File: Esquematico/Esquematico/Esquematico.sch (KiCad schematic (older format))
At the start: 27 parts, among them P1 Digital, P10 CONN_01X01, P11 CONN_01X01, P12 CONN_01X01, P13 CONN_01X01, P2 Power, P3 Analog, P4 Analog, P5 PWM, P6 PWM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

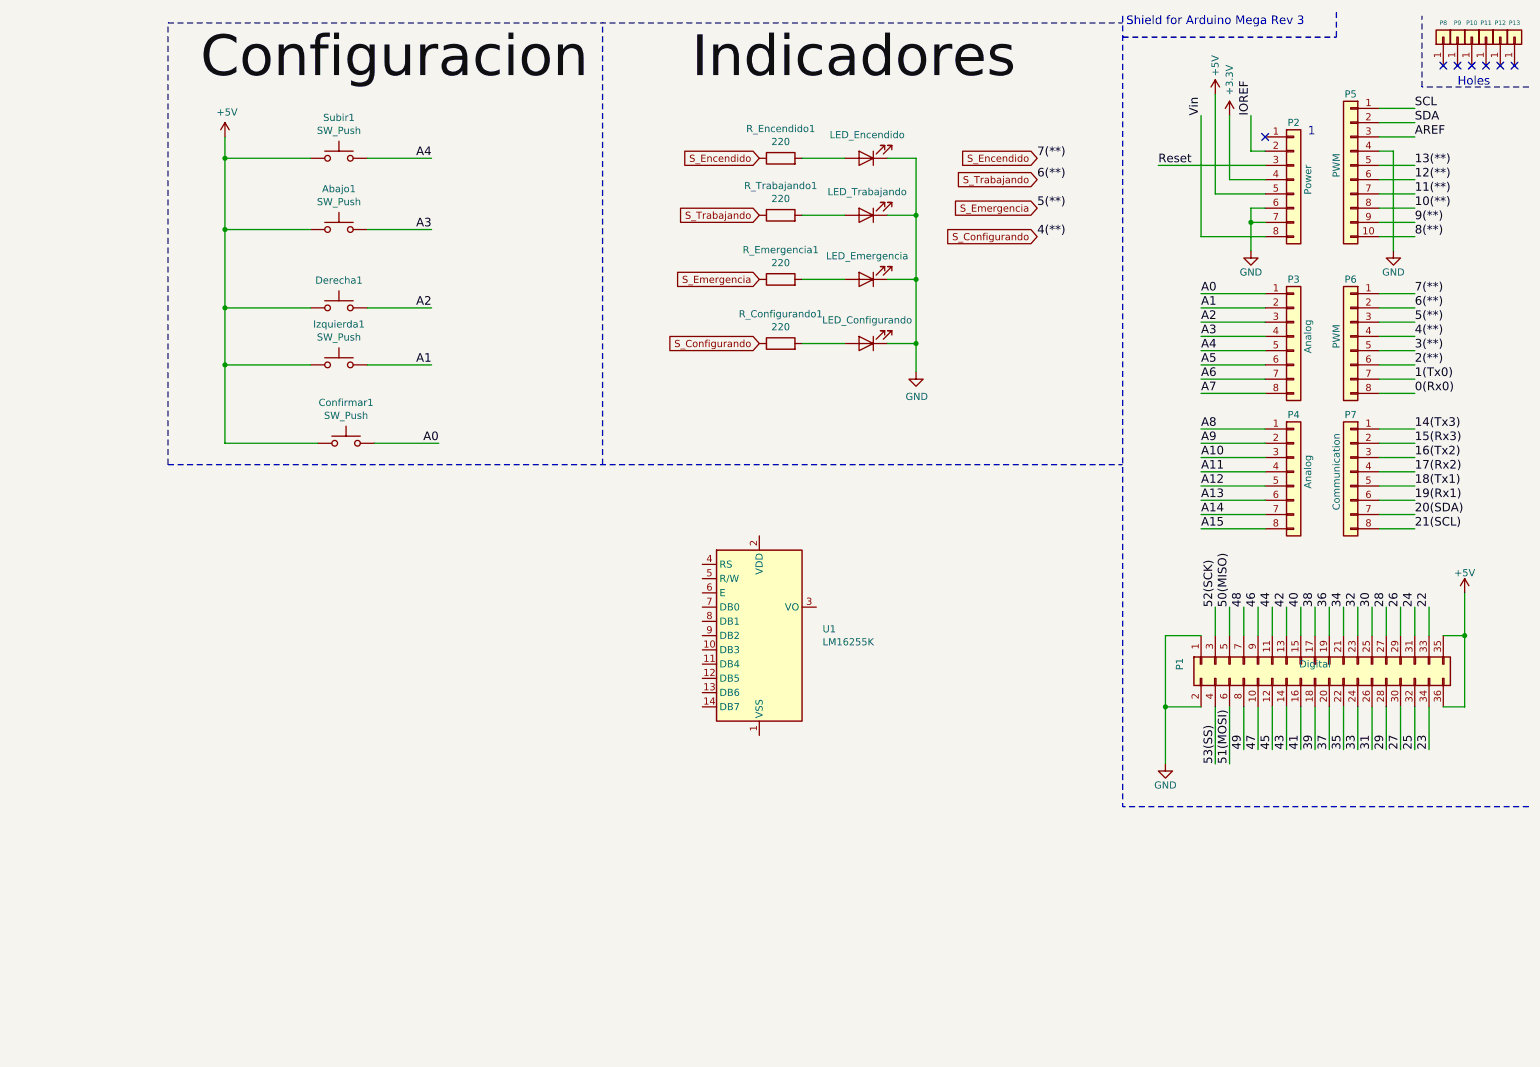
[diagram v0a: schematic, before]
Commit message: version 0.31 las conexiones provadas ya estan en esquematico
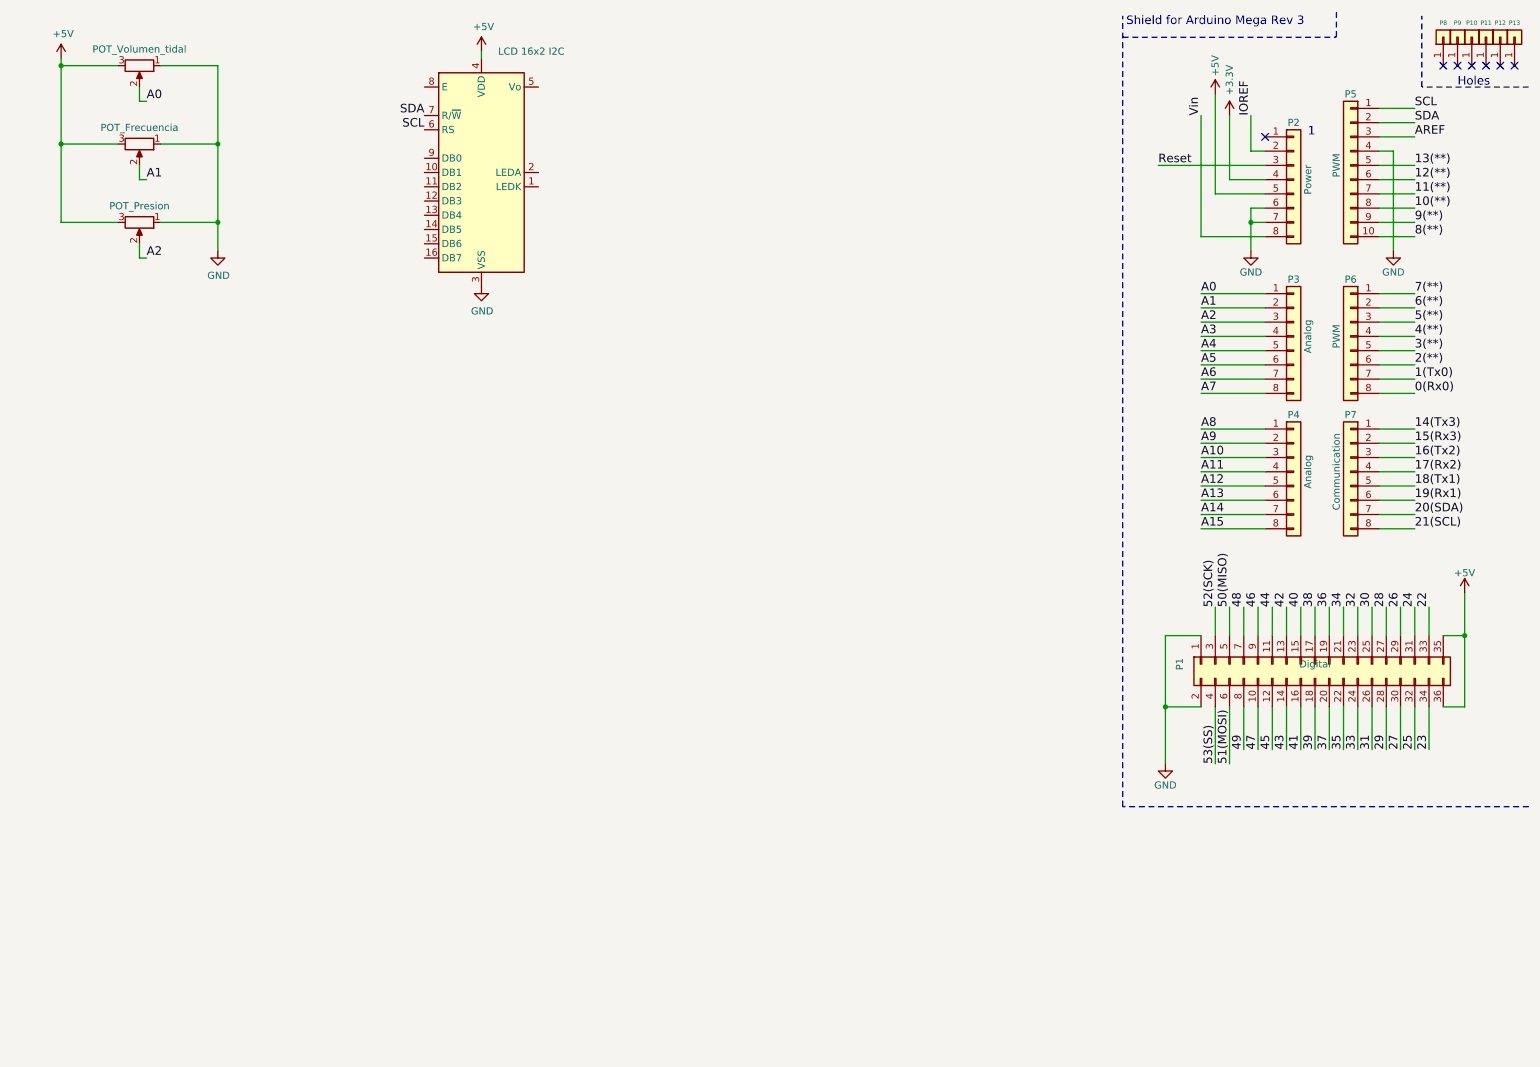
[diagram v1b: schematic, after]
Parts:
- removed Abajo1, Confirmar1, Izquierda1, Subir1: SW_Push, Button_Switch_THT:SW_PUSH_6mm, symbol Switch:SW_Push
- removed D1: LED_Encendido, LED_THT:LED_D3.0mm, symbol Device:LED
- removed D2: LED_Trabajando, LED_THT:LED_D3.0mm, symbol Device:LED
- removed D3: LED_Emergencia, LED_THT:LED_D3.0mm, symbol Device:LED
- removed D4: LED_Configurando, LED_THT:LED_D3.0mm, symbol Device:LED
- removed Derecha1: Derecha, Button_Switch_THT:SW_PUSH_6mm, symbol Switch:SW_Push
- removed R_Configurando1, R_Emergencia1, R_Encendido1, R_Trabajando1: 220, Resistor_THT:R_Axial_DIN0309_L9.0mm_D3.2mm_P20.32mm_Horizontal, symbol Device:R
- removed U1: LM16255K, Display:Adafruit_SSD1306_No_Mounting_Holes, symbol Display_Character:LM16255K
- added DS1: LCD 16x2 I2C, Display:HY1602E, symbol Display_Character:HY1602E
- added RV1: POT_Volumen_tidal, Potentiometer_THT:Potentiometer_Piher_PC-16_Single_Horizontal, symbol Device:R_POT
- added RV2: POT_Frecuencia, Potentiometer_THT:Potentiometer_Piher_PC-16_Single_Horizontal, symbol Device:R_POT
- added RV3: POT_Presion, Potentiometer_THT:Potentiometer_Piher_PC-16_Single_Horizontal, symbol Device:R_POT
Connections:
- net +5V: now also DS1.4 (VDD), RV1.3, RV2.3, RV3.3
- net A0: now also RV1.2
- net A1: now also RV2.2
- net A2: now also RV3.2
- net GND: now also DS1.3 (VSS), RV1.1, RV2.1, RV3.1
- net SCL: now also DS1.6 (RS)
- net SDA: now also DS1.7 (R/~W)
- net S_Configurando renamed 4(**)
- net S_Emergencia renamed 5(**)
- net S_Encendido renamed 7(**)
- net S_Trabajando renamed 6(**)

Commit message: Diseño esquematico para presenstacion
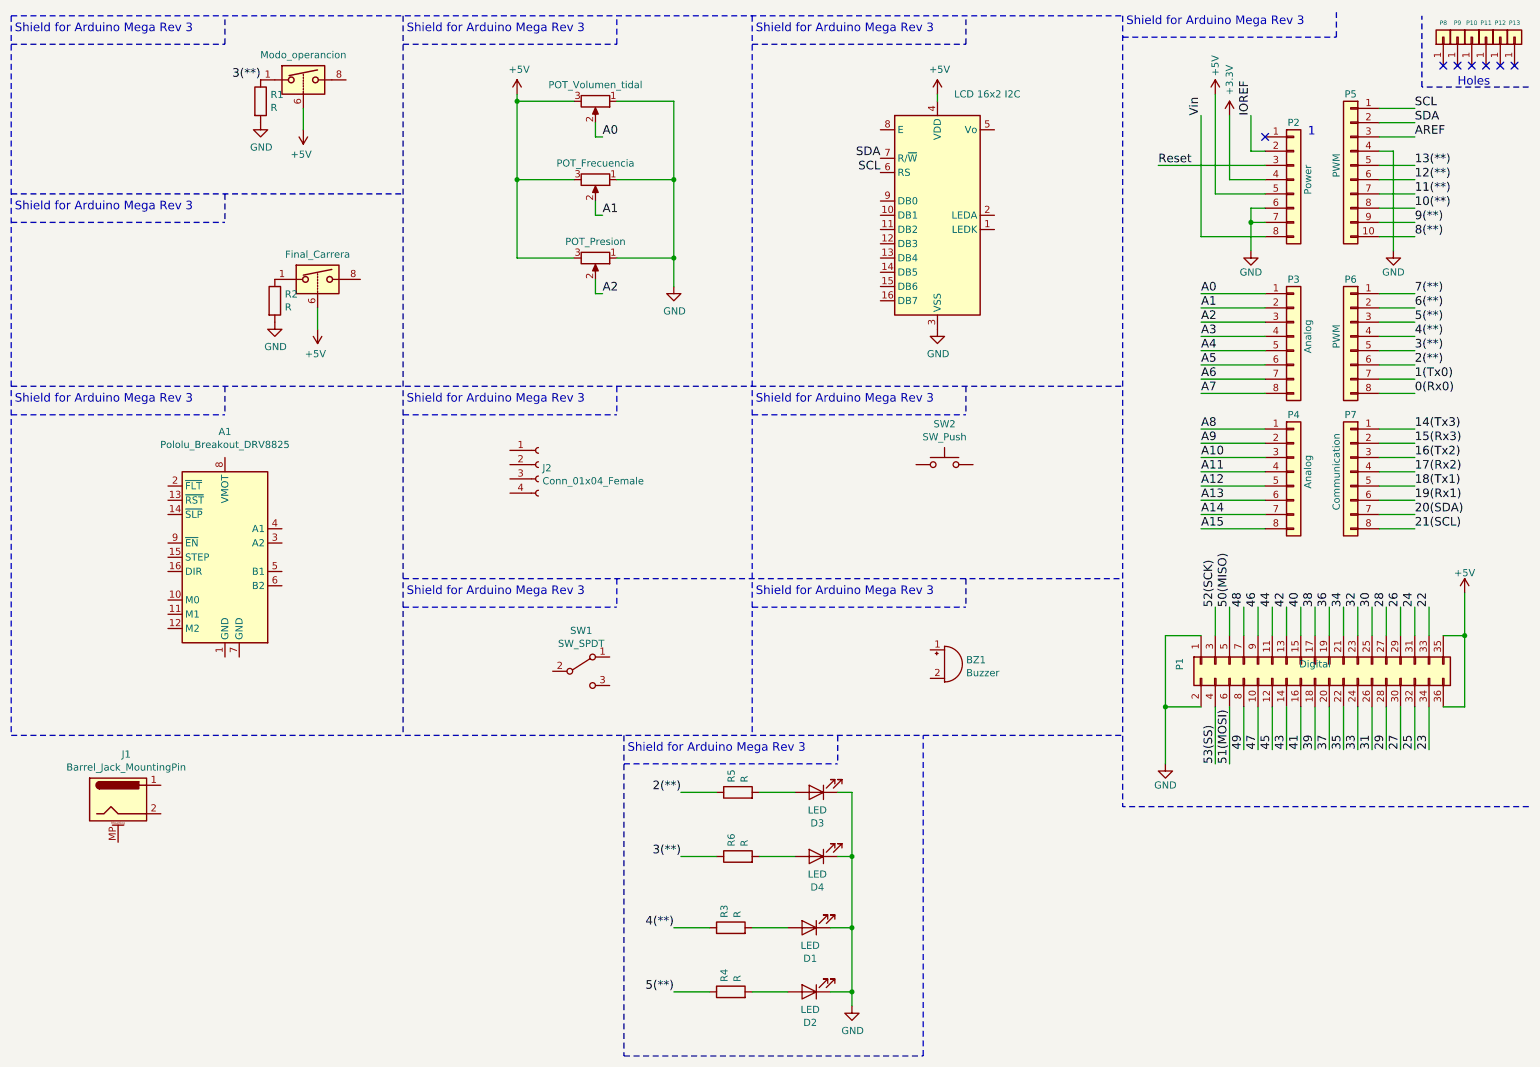
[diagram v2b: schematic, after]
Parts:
- added A1: Pololu_Breakout_DRV8825, Module:Pololu_Breakout-16_15.2x20.3mm, symbol Driver_Motor:Pololu_Breakout_DRV8825
- added BZ1: Buzzer, Buzzer_Beeper:MagneticBuzzer_ProSignal_ABI-010-RC, symbol Device:Buzzer
- added D1, D2, D3, D4: LED, LED_THT:LED_D3.0mm, symbol Device:LED
- added Final_Carrera_switch1: Final_Carrera, Package_DIP:DIP-8_W7.62mm, symbol Analog_Switch:DG418LDJ
- added J1: Barrel_Jack_MountingPin, Connector_BarrelJack:BarrelJack_CUI_PJ-102AH_Horizontal, symbol Connector:Barrel_Jack_MountingPin
- added J2: Conn_01x04_Female, Connector_Molex:Molex_KK-396_A-41791-0004_1x04_P3.96mm_Vertical, symbol Connector:Conn_01x04_Female
- added Modo_Operacion_switch1: Modo_operancion, Package_DIP:DIP-8_W7.62mm, symbol Analog_Switch:DG418LDJ
- added R1: R, Resistor_THT:R_Axial_DIN0309_L9.0mm_D3.2mm_P12.70mm_Horizontal, symbol Device:R
- added R2, R3, R4, R5, R6: R, Resistor_THT:R_Axial_DIN0516_L15.5mm_D5.0mm_P20.32mm_Horizontal, symbol Device:R
- added SW1: SW_SPDT, Button_Switch_THT:SW_E-Switch_EG1224_SPDT_Angled, symbol Switch:SW_SPDT
- added SW2: SW_Push, Button_Switch_THT:SW_PUSH_6mm, symbol Switch:SW_Push
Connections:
- net +5V: now also Final_Carrera_switch1.6, Modo_Operacion_switch1.6
- net 2(**): now also R5.1
- net 3(**): now also Modo_Operacion_switch1.1, R1.1, R6.1
- net 4(**): now also R3.1
- net 5(**): now also R4.1
- net GND: now also D1.1 (K), D2.1 (K), D3.1 (K), D4.1 (K), R1.2, R2.2
- new net: Final_Carrera_switch1.1, R2.1
- new net: D3.2 (A), R5.2
- new net: D4.2 (A), R6.2
- new net: D1.2 (A), R3.2
- new net: D2.2 (A), R4.2
